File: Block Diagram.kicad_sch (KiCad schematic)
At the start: 38 parts, among them J1001 Header, J701 ZHOURI DC3, J800 Molex 430451227, J901 Header

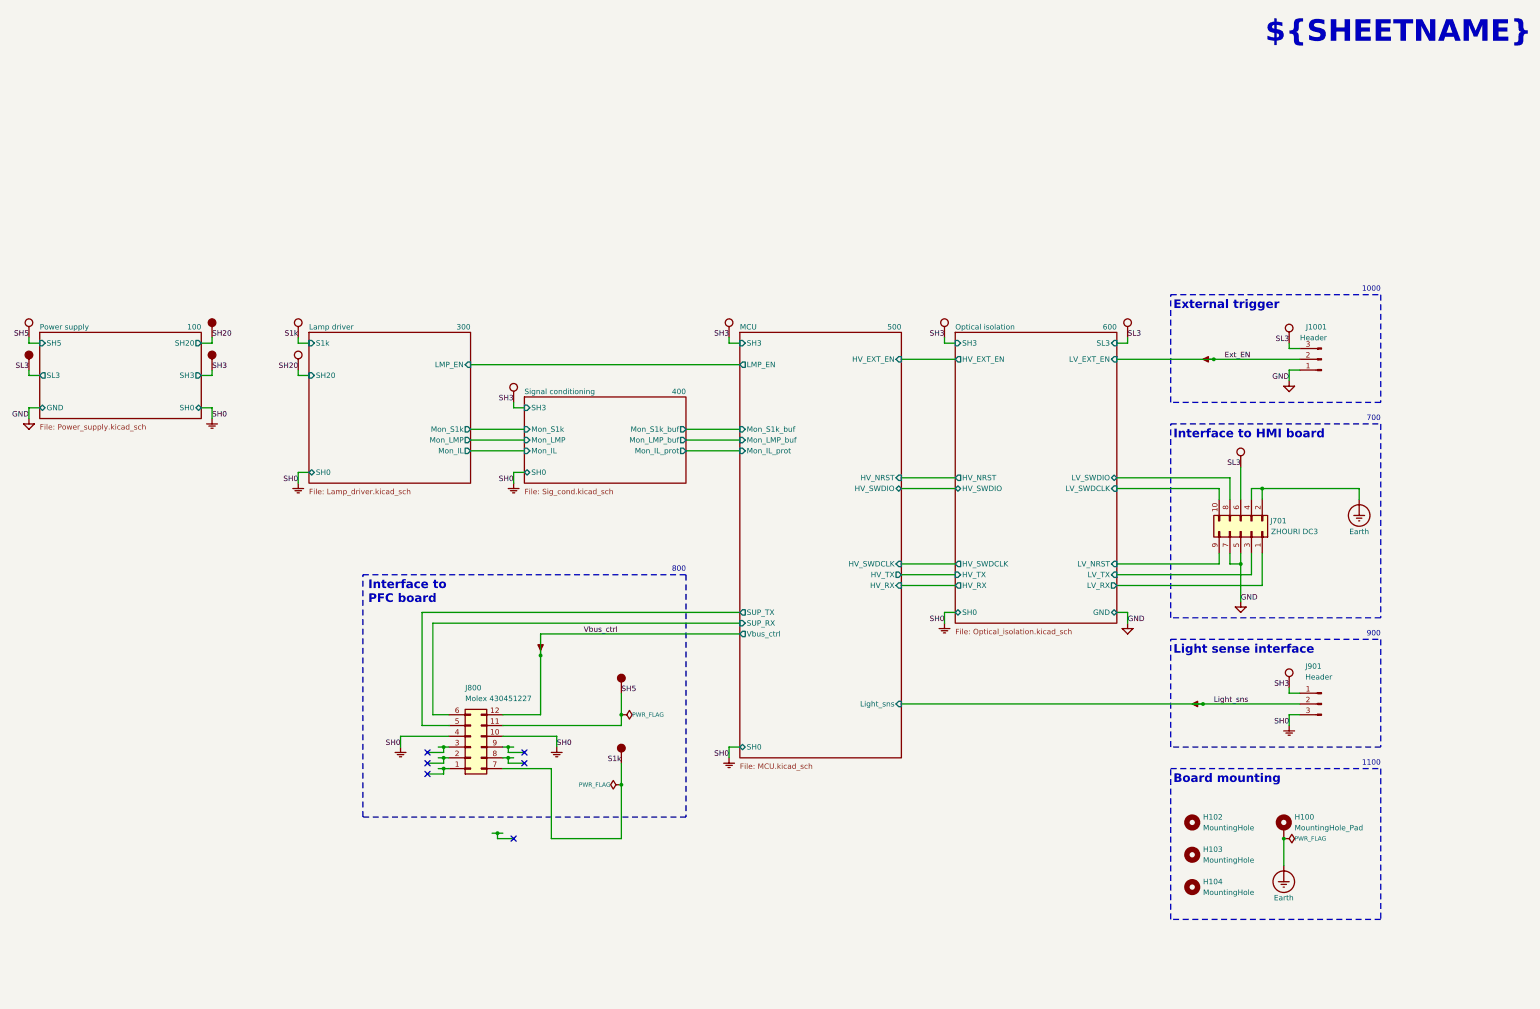
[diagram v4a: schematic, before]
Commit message: Reannotated, silk done, missing some 3D models
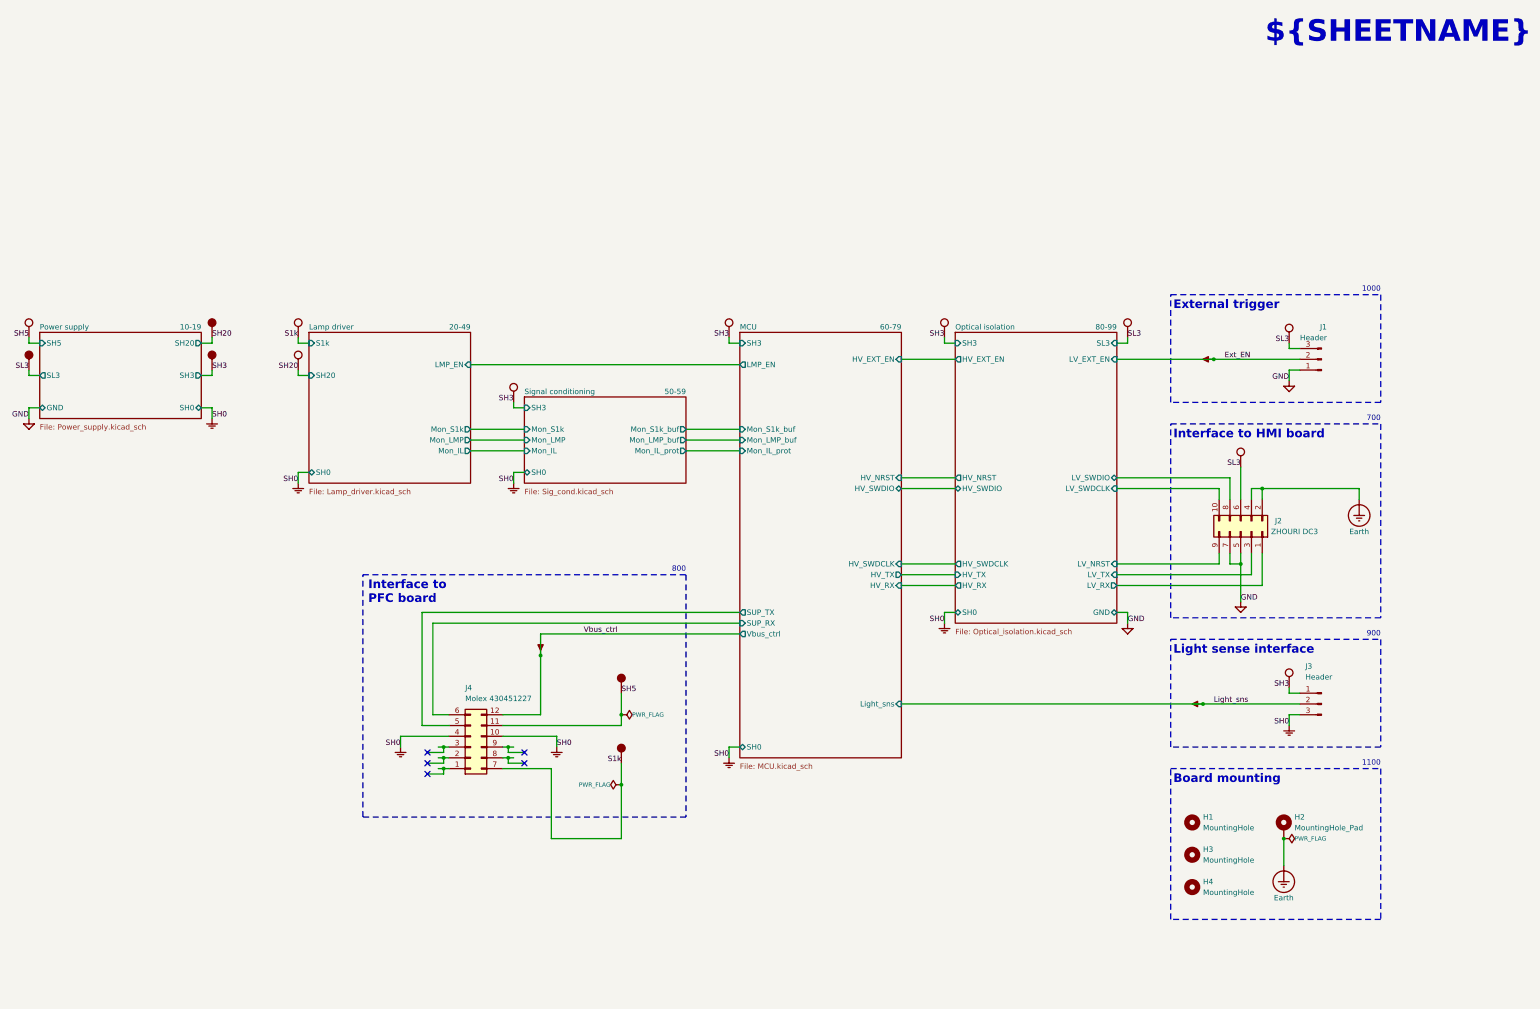
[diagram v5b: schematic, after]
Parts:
- renumbered H102 to H1, H100 to H2, H103 to H3, H104 to H4, J1001 to J1, J701 to J2, J901 to J3, J800 to J4, P848 to P1, P787 to P10, P786 to P11, P847 to P12, P359 to P13, P315 to P14, P310 to P15, P309 to P16, P701 to P17, P799 to P18, P800 to P19, P785 to P2, P702 to P20, P803 to P21, P320 to P22, P8 to P23, P4 to P24, P5 to P25, P328 to P26, P802 to P27, P15 to P28, P139 to P29, P801 to P30, P11 to P31, P846 to P4, P852 to P5, P853 to P6, P854 to P7, P352 to P8, P358 to P9
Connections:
- no-connect marks 6 -> 5
